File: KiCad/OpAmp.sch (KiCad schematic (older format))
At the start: 7 parts

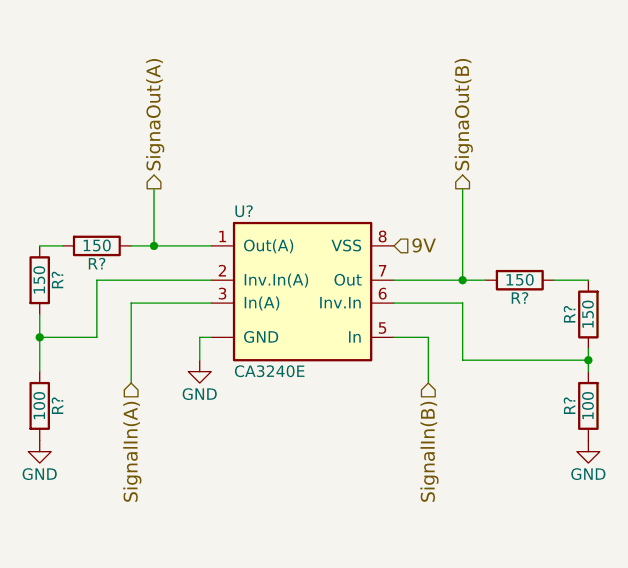
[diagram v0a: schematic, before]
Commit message: Updated the schematics and started with the PCB
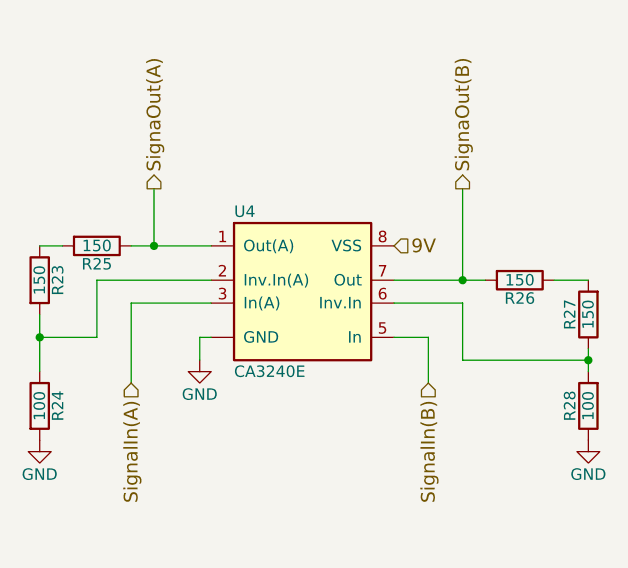
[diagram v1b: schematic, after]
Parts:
- R23, R24, R25, R26, R27, R28: renamed from R?; footprint (none) -> Resistors_ThroughHole:Resistor_Vertical_RM5mm
- gave numbers to parts that had none: 1
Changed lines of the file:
@@
 $EndDescr
 $Comp
-L CA3240E U?
+L CA3240E U4
 U 1 1 5718642F
 P 4150 1900
-F 0 "U?" H 3850 2250 50  0000 L CNN
+F 0 "U4" H 3850 2250 50  0000 L CNN
 F 1 "CA3240E" H 3850 1550 50  0000 L CNN
-F 2 "" H 4150 1900 50  0000 C CNN
+F 2 "" H 4150 1900 50  0001 C CNN
 F 3 "" H 4150 1900 50  0000 C CNN
 	1    4150 1900
@@
 SignalIn(B)
 $Comp
-L R R?
+L R R25
 U 1 1 571877CF
 P 3250 1700
-F 0 "R?" V 3330 1700 50  0000 C CNN
+F 0 "R25" V 3330 1700 50  0000 C CNN
 F 1 "150" V 3250 1700 50  0000 C CNN
-F 2 "" V 3180 1700 50  0000 C CNN
+F 2 "Resistors_ThroughHole:Resistor_Vertical_RM5mm" V 3180 1700 50  0001 C CNN
 F 3 "" H 3250 1700 50  0000 C CNN
 	1    3250 1700
@@
 $EndComp
 $Comp
-L R R?
+L R R24
 U 1 1 57187832
 P 3000 2400
-F 0 "R?" V 3080 2400 50  0000 C CNN
+F 0 "R24" V 3080 2400 50  0000 C CNN
 F 1 "100" V 3000 2400 50  0000 C CNN
-F 2 "" V 2930 2400 50  0000 C CNN
+F 2 "Resistors_ThroughHole:Resistor_Vertical_RM5mm" V 2930 2400 50  0001 C CNN
 F 3 "" H 3000 2400 50  0000 C CNN
 	1    3000 2400
@@
 $EndComp
 $Comp
-L GND #PWR?
+L GND #PWR020
 U 1 1 571879D5
 P 3000 2550
-F 0 "#PWR?" H 3000 2300 50  0001 C CNN
+F 0 "#PWR020" H 3000 2300 50  0001 C CNN
 F 1 "GND" H 3000 2400 50  0000 C CNN
 F 2 "" H 3000 2550 50  0000 C CNN
@@
 $EndComp
 $Comp
-L GND #PWR?
+L GND #PWR021
 U 1 1 571879F0
 P 3700 2200
-F 0 "#PWR?" H 3700 1950 50  0001 C CNN
+F 0 "#PWR021" H 3700 1950 50  0001 C CNN
 F 1 "GND" H 3700 2050 50  0000 C CNN
 F 2 "" H 3700 2200 50  0000 C CNN
@@
 	4550 1850 4950 1850
 $Comp
-L R R?
+L R R26
 U 1 1 57187D93
 P 5100 1850
-F 0 "R?" V 5180 1850 50  0000 C CNN
+F 0 "R26" V 5180 1850 50  0000 C CNN
 F 1 "150" V 5100 1850 50  0000 C CNN
-F 2 "" V 5030 1850 50  0000 C CNN
+F 2 "Resistors_ThroughHole:Resistor_Vertical_RM5mm" V 5030 1850 50  0001 C CNN
 F 3 "" H 5100 1850 50  0000 C CNN
 	1    5100 1850
@@
 Connection ~ 4850 1850
 $Comp
-L GND #PWR?
+L GND #PWR022
 U 1 1 57187F37
 P 5400 2550
-F 0 "#PWR?" H 5400 2300 50  0001 C CNN
+F 0 "#PWR022" H 5400 2300 50  0001 C CNN
 F 1 "GND" H 5400 2400 50  0000 C CNN
 F 2 "" H 5400 2550 50  0000 C CNN
@@
 	4850 1950 4850 2200
 $Comp
-L R R?
+L R R28
 U 1 1 571881CA
 P 5400 2400
-F 0 "R?" V 5480 2400 50  0000 C CNN
+F 0 "R28" V 5480 2400 50  0000 C CNN
 F 1 "100" V 5400 2400 50  0000 C CNN
-F 2 "" V 5330 2400 50  0000 C CNN
+F 2 "Resistors_ThroughHole:Resistor_Vertical_RM5mm" V 5330 2400 50  0001 C CNN
 F 3 "" H 5400 2400 50  0000 C CNN
 	1    5400 2400
@@
 $EndComp
 $Comp
-L R R?
+L R R27
 U 1 1 57188573
 P 5400 2000
-F 0 "R?" V 5480 2000 50  0000 C CNN
+F 0 "R27" V 5480 2000 50  0000 C CNN
 F 1 "150" V 5400 2000 50  0000 C CNN
-F 2 "" V 5330 2000 50  0000 C CNN
+F 2 "Resistors_ThroughHole:Resistor_Vertical_RM5mm" V 5330 2000 50  0001 C CNN
 F 3 "" H 5400 2000 50  0000 C CNN
 	1    5400 2000
@@
 Connection ~ 5400 2200
 $Comp
-L R R?
+L R R23
 U 1 1 57188968
 P 3000 1850
-F 0 "R?" V 3080 1850 50  0000 C CNN
+F 0 "R23" V 3080 1850 50  0000 C CNN
 F 1 "150" V 3000 1850 50  0000 C CNN
-F 2 "" V 2930 1850 50  0000 C CNN
+F 2 "Resistors_ThroughHole:Resistor_Vertical_RM5mm" V 2930 1850 50  0001 C CNN
 F 3 "" H 3000 1850 50  0000 C CNN
 	1    3000 1850
